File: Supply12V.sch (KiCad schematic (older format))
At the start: 31 parts, among them Q3 BSS138, Q5 CSD18504Q5A, Q6 CSD18504Q5A, U6 LM25116MHX

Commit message: Reannotated parts
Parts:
- renumbered C25 to C13, C19 to C14, C23 to C15, C13 to C16, C3 to C17, C20 to C18, C28 to C19, C11 to C20, C14 to C21, C21 to C22, D1 to D3, L1 to L2, Q5 to Q7, Q3 to Q8, Q6 to Q9, R33 to R59, R34 to R60, R16 to R61, R19 to R62, R23 to R63, R29 to R64, R17 to R65, R83 to R66, R36 to R67, R30 to R68, R24 to R69, R27 to R70, U6 to U1, W2 to W1, W1 to W2

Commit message: Silkscreen and 3D touchups
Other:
- moved on the sheet: C13, C14, C15, C16, C17, C18, C19, C20, C21, C22, D3, JP1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

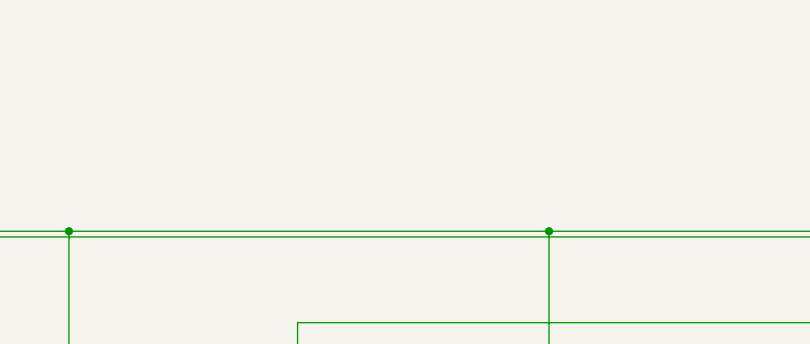
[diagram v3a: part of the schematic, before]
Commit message: Researched alternative DC-DC controllers
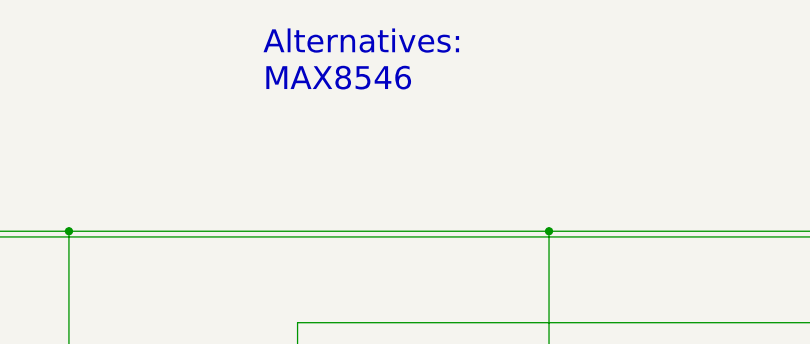
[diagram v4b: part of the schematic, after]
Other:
- note added: "Alternatives:\nMAX8546"
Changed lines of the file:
@@
 Wire Wire Line
 	1025 1425 1000 1400
+Text Notes 3550 800  0    100  ~ 0
+Alternatives:\nMAX8546
 $EndSCHEMATC

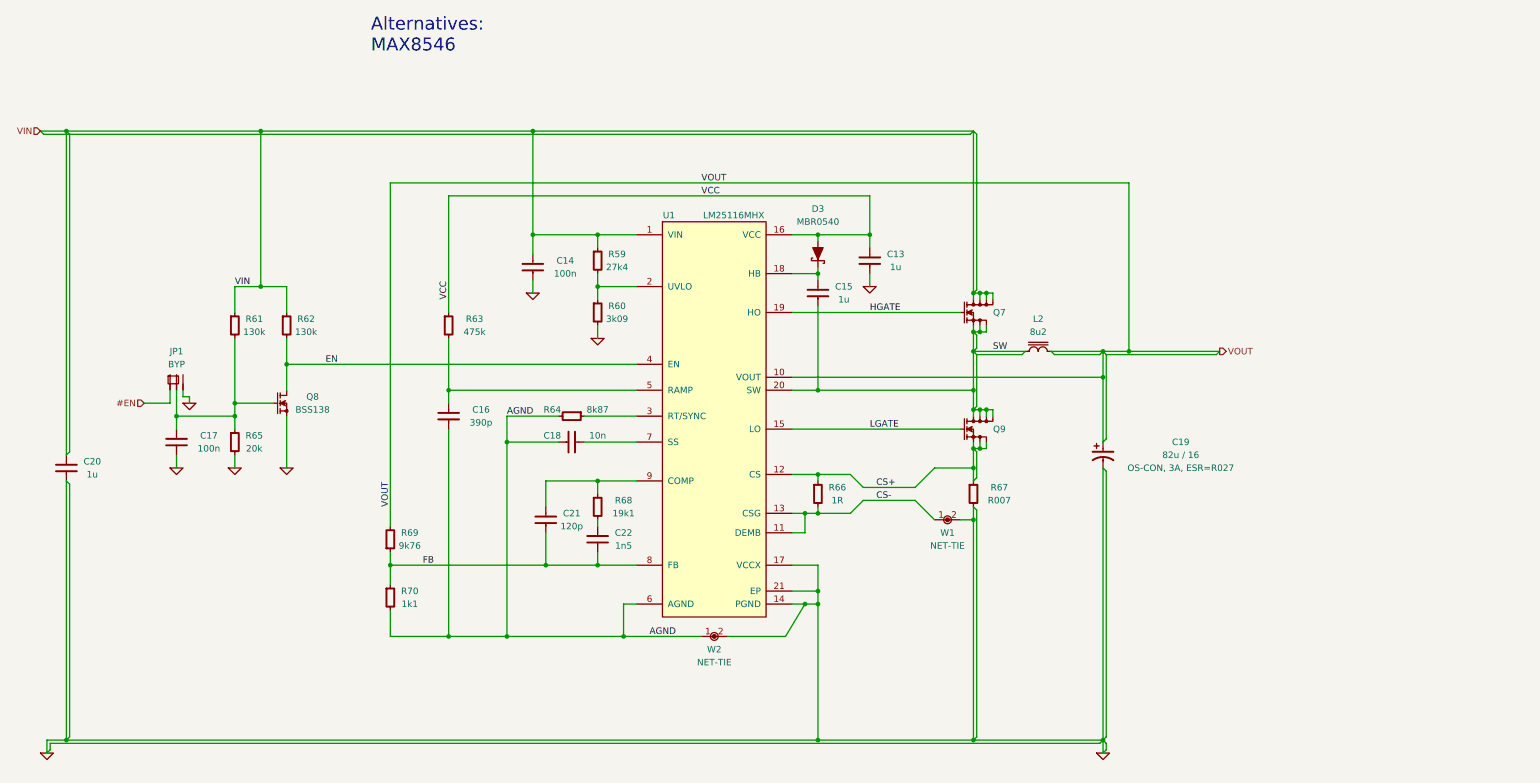
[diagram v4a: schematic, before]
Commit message: Changed BSS138 to MMUN221
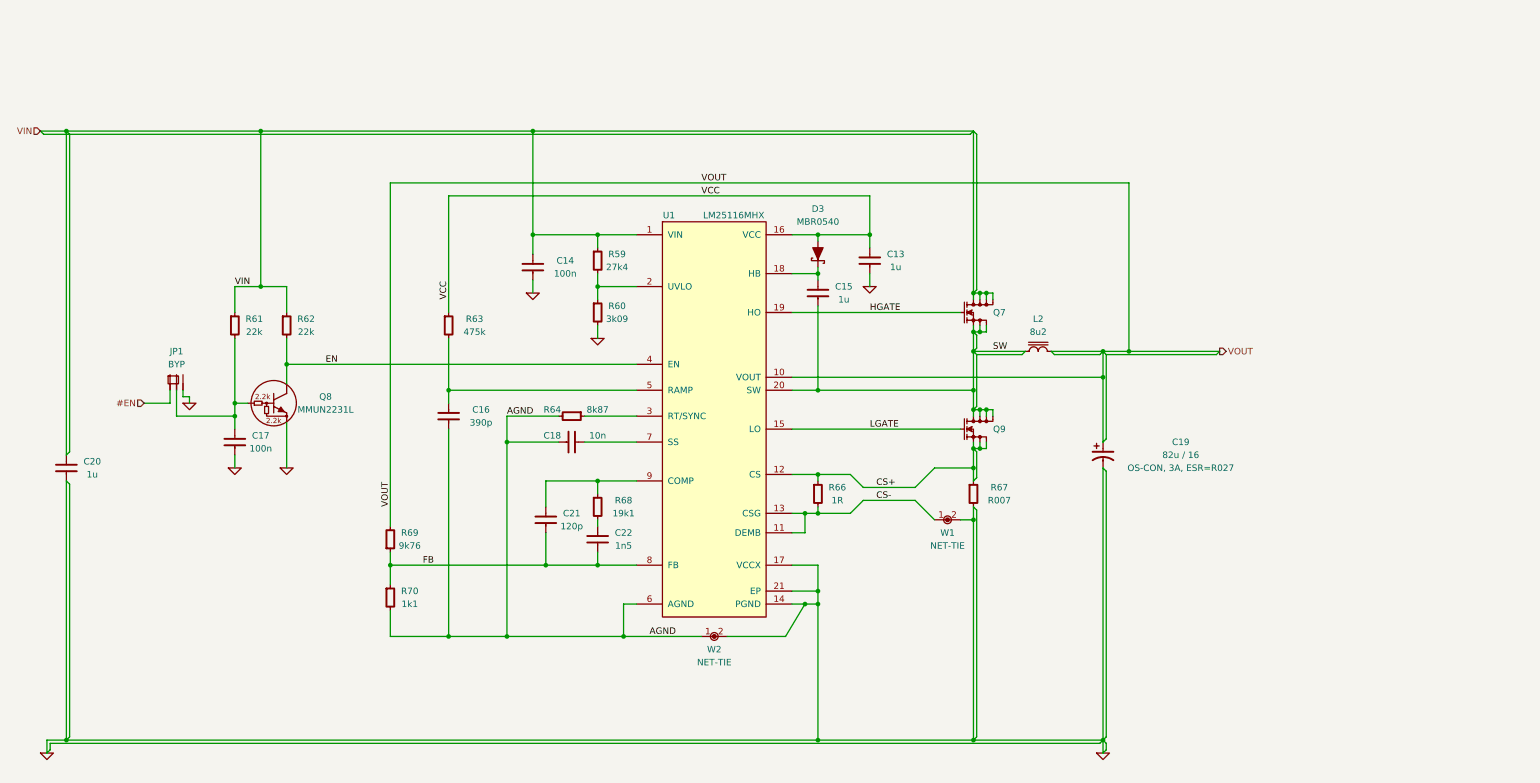
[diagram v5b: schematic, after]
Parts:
- removed Q8: BSS138, smd-semi:SOT-23, symbol BSS138
- removed R65: 20k, IPC7351-Nominal:RESC1005X40, symbol R-0402
- added Q8: MMUN2231L, smd-semi:SOT-23, symbol MMUN2231L
- R61, R62: value 130k -> 22k
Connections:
- net EN: now also Q8.3
- net GND: now also Q8.2
- net at C17.1, JP1.2, R61.2: now also Q8.1
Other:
- note removed: "Alternatives:\nMAX8546"
- moved on the sheet: C17
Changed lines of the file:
@@
-$EndComp
-$Comp
-L BSS138 Q8
-U 1 1 54D806F7
-P 2850 3500
-F 0 "Q8" H 3100 3550 50  0000 C CNN
-F 1 "BSS138" H 3100 3450 50  0000 C CNN
-F 2 "smd-semi:SOT-23" H 2850 3500 50  0001 C CNN
-F 3 "" H 2850 3500 60  0000 C CNN
-F 4 "Q3" H 2850 3500 50  0001 C CNN "OldReference"
-	1    2850 3500
-	1    0    0    -1
 $EndComp
 $Comp
@@
 P 2500 2900
 F 0 "R61" H 2650 2950 50  0000 C CNN
-F 1 "130k" H 2650 2850 50  0000 C CNN
+F 1 "22k" H 2650 2850 50  0000 C CNN
 F 2 "IPC7351-Nominal:RESC1005X40" H 2500 2900 50  0001 C CNN
 F 3 "" H 2500 2950 60  0000 C CNN
@@
 $EndComp
 $Comp
-L R-0402 R65
-U 1 1 54D80707
-P 2500 3800
-F 0 "R65" H 2650 3850 50  0000 C CNN
-F 1 "20k" H 2650 3750 50  0000 C CNN
-F 2 "IPC7351-Nominal:RESC1005X40" H 2500 3800 50  0001 C CNN
-F 3 "" H 2500 3850 60  0000 C CNN
-F 4 "R17" H 2500 3800 50  0001 C CNN "OldReference"
-	1    2500 3800
-	1    0    0    -1
-$EndComp
-$Comp
 L R-0402 R62
 U 1 1 54D8071F
 P 2900 2900
 F 0 "R62" H 3050 2950 50  0000 C CNN
-F 1 "130k" H 3050 2850 50  0000 C CNN
+F 1 "22k" H 3050 2850 50  0000 C CNN
 F 2 "IPC7351-Nominal:RESC1005X40" H 2900 2900 50  0001 C CNN
 F 3 "" H 2900 2950 60  0000 C CNN
@@
 L C-0805 C17
 U 1 1 54D8072E
-P 2050 3800
-F 0 "C17" H 2300 3850 50  0000 C CNN
-F 1 "100n" H 2300 3750 50  0000 C CNN
-F 2 "IPC7351-Nominal:CAPC2012X70" H 2050 3800 50  0001 C CNN
-F 3 "" H 2040 3775 60  0000 C CNN
-F 4 "C3" H 2050 3800 50  0001 C CNN "OldReference"
-	1    2050 3800
+P 2500 3800
+F 0 "C17" H 2700 3850 50  0000 C CNN
+F 1 "100n" H 2700 3750 50  0000 C CNN
+F 2 "IPC7351-Nominal:CAPC2012X70" H 2500 3800 50  0001 C CNN
+F 3 "" H 2490 3775 60  0000 C CNN
+F 4 "C3" H 2500 3800 50  0001 C CNN "OldReference"
+	1    2500 3800
 	1    0    0    -1
 $EndComp
@@
 	1    0    0    -1
 $EndComp
-$Comp
-L GND #PWR0225
-U 1 1 54DA9586
-P 2050 4000
-F 0 "#PWR0225" H 2050 4000 30  0001 C CNN
-F 1 "GND" H 2050 3930 30  0001 C CNN
-F 2 "" H 2050 4000 60  0000 C CNN
-F 3 "" H 2050 4000 60  0000 C CNN
-F 4 "#PWR0223" H 2050 4000 50  0001 C CNN "OldReference"
-	1    2050 4000
-	1    0    0    -1
-$EndComp
 Text HLabel 1000 1400 0    50   Input ~ 0
 VIN
@@
 VCC
 $Comp
-L GND #PWR0226
+L GND #PWR0225
 U 1 1 54DAF58D
 P 1050 6200
-F 0 "#PWR0226" H 1050 6200 30  0001 C CNN
+F 0 "#PWR0225" H 1050 6200 30  0001 C CNN
 F 1 "GND" H 1050 6130 30  0001 C CNN
 F 2 "" H 1050 6200 60  0000 C CNN
@@
 $EndComp
 Wire Wire Line
-	8200 2900 8200 2950
-Wire Wire Line
-	8200 2950 8200 3100
-Wire Wire Line
-	8200 3100 8200 3400
-Wire Wire Line
-	8200 3400 8200 3550
-Wire Wire Line
-	8200 3550 8200 3600
-Wire Wire Line
-	8200 3800 8200 3850
-Wire Wire Line
-	8200 3850 8200 4000
-Wire Wire Line
-	8200 4000 8200 4100
+	8200 2900 8200 3600
+Wire Wire Line
+	8200 3800 8200 4100
 Wire Wire Line
 	5300 4400 5300 4450
 Wire Wire Line
-	9200 4000 9200 6100
-Wire Wire Line
-	9200 6100 9200 6200
-Wire Wire Line
-	8200 1400 8200 2650
-Wire Wire Line
-	8200 2650 8200 2700
-Wire Wire Line
-	8200 2650 8250 2650
-Wire Wire Line
-	8250 2650 8300 2650
-Wire Wire Line
-	8300 2650 8350 2650
+	9200 4000 9200 6200
+Wire Wire Line
+	8200 1400 8200 2700
+Wire Wire Line
+	8200 2650 8350 2650
 Wire Wire Line
 	8250 2650 8250 2700
@@
 	8250 2900 8250 2950
 Wire Wire Line
-	8200 2950 8250 2950
-Wire Wire Line
-	8250 2950 8300 2950
+	8200 2950 8300 2950
 Connection ~ 8200 2950
 Wire Wire Line
@@
 Connection ~ 8250 2950
 Wire Wire Line
-	8200 3550 8250 3550
-Wire Wire Line
-	8250 3550 8300 3550
-Wire Wire Line
-	8300 3550 8350 3550
+	8200 3550 8350 3550
 Wire Wire Line
 	8250 3550 8250 3600
@@
 	8250 3800 8250 3850
 Wire Wire Line
-	8200 3850 8250 3850
-Wire Wire Line
-	8250 3850 8300 3850
+	8200 3850 8300 3850
 Connection ~ 8200 3850
 Wire Wire Line
@@
 Connection ~ 8250 3850
 Wire Wire Line
-	8800 3100 9200 3100
-Wire Wire Line
-	9200 3100 9400 3100
-Wire Wire Line
-	9400 3100 10100 3100
-Wire Wire Line
-	9200 3100 9200 3300
-Wire Wire Line
-	9200 3300 9200 3800
+	8800 3100 10100 3100
+Wire Wire Line
+	9200 3100 9200 3800
 Wire Wire Line
 	8600 3100 8200 3100
 Wire Wire Line
-	1050 6100 1200 6100
-Wire Wire Line
-	1200 6100 7000 6100
-Wire Wire Line
-	7000 6100 8200 6100
-Wire Wire Line
-	8200 6100 9200 6100
-Wire Wire Line
-	8200 4300 8200 4400
-Wire Wire Line
-	8200 4400 8200 6100
+	1050 6100 9200 6100
+Wire Wire Line
+	8200 4300 8200 6100
 Connection ~ 9200 6100
 Connection ~ 8200 3100
@@
 	1200 1400 1200 3900
 Wire Wire Line
-	1000 1400 1200 1400
-Wire Wire Line
-	1200 1400 2700 1400
-Wire Wire Line
-	2700 1400 4800 1400
-Wire Wire Line
-	4800 1400 8200 1400
+	1000 1400 8200 1400
 Connection ~ 1200 1400
 Connection ~ 1200 6100
@@
 	8100 4400 8200 4400
 Wire Wire Line
-	6800 3400 7000 3400
-Wire Wire Line
-	7000 3400 8200 3400
+	6800 3400 8200 3400
 Wire Wire Line
 	6800 3700 8100 3700
@@
 Connection ~ 7000 4950
 Wire Wire Line
-	7000 5050 6900 5050
-Wire Wire Line
-	6900 5050 6800 5050
+	7000 5050 6800 5050
 Connection ~ 7000 5050
 Wire Wire Line
@@
 	6800 2500 7000 2500
 Wire Wire Line
-	7000 2450 7000 2500
-Wire Wire Line
-	7000 2500 7000 2550
-Wire Wire Line
-	6800 2200 7000 2200
-Wire Wire Line
-	7000 2200 7400 2200
+	7000 2450 7000 2550
+Wire Wire Line
+	6800 2200 7400 2200
 Wire Wire Line
 	7000 2200 7000 2250
@@
 	7400 2600 7400 2500
 Wire Wire Line
-	7400 1900 7400 2200
-Wire Wire Line
-	7400 2200 7400 2300
+	7400 1900 7400 2300
 Connection ~ 7000 2200
 Wire Wire Line
-	5300 2500 5300 2600
-Wire Wire Line
-	5300 2600 5300 2700
+	5300 2500 5300 2700
 Wire Wire Line
 	5300 2600 5600 2600
@@
 	7350 4150 7250 4050
 Wire Wire Line
-	7250 4050 7000 4050
-Wire Wire Line
-	7000 4050 6800 4050
+	7250 4050 6800 4050
 Wire Wire Line
 	7000 4100 7000 4050
@@
 	7350 4250 7250 4350
 Wire Wire Line
-	7250 4350 7000 4350
-Wire Wire Line
-	7000 4350 6900 4350
-Wire Wire Line
-	6900 4350 6800 4350
+	7250 4350 6800 4350
 Wire Wire Line
 	7000 4300 7000 4350
@@
 Connection ~ 6900 5050
 Wire Wire Line
-	3700 5300 4150 5300
-Wire Wire Line
-	4150 5300 4600 5300
-Wire Wire Line
-	4600 5300 5500 5300
-Wire Wire Line
-	5500 5300 6100 5300
+	3700 5300 6100 5300
 Wire Wire Line
 	5500 5300 5500 5050
@@
 	5500 5050 5600 5050
 Wire Wire Line
-	4900 4100 5300 4100
-Wire Wire Line
-	5300 4100 5600 4100
+	4900 4100 5600 4100
 Wire Wire Line
 	4900 4100 4900 4300
@@
 	5300 4750 5300 4650
 Wire Wire Line
-	3700 4750 4900 4750
-Wire Wire Line
-	4900 4750 5300 4750
-Wire Wire Line
-	5300 4750 5600 4750
+	3700 4750 5600 4750
 Wire Wire Line
 	4900 4750 4900 4500
@@
 Connection ~ 5500 5300
 Wire Wire Line
-	3700 4650 3700 4750
-Wire Wire Line
-	3700 4750 3700 4900
+	3700 4650 3700 4900
 Connection ~ 4900 4750
 Connection ~ 3700 4750
@@
 	5000 3600 4600 3600
 Wire Wire Line
-	4600 3600 4600 3800
-Wire Wire Line
-	4600 3800 4600 5300
+	4600 3600 4600 5300
 Connection ~ 4600 5300
 Wire Wire Line
@@
 Connection ~ 4150 5300
 Wire Wire Line
-	4150 3000 4150 3400
-Wire Wire Line
-	4150 3400 4150 3500
+	4150 3000 4150 3500
 Wire Wire Line
 	4150 3400 5600 3400
@@
 	5600 3200 2900 3200
 Wire Wire Line
-	2900 3000 2900 3200
-Wire Wire Line
-	2900 3200 2900 3400
+	2900 3000 2900 3350
 Connection ~ 2900 3200
 Wire Wire Line
-	2500 3000 2500 3500
-Wire Wire Line
-	2500 3500 2500 3600
-Wire Wire Line
-	2500 3600 2500 3700
-Wire Wire Line
-	2500 3500 2800 3500
+	2500 3500 2600 3500
 Connection ~ 2500 3500
 Wire Wire Line
 	2500 3600 2050 3600
-Wire Wire Line
-	2050 3400 2050 3600
-Wire Wire Line
-	2050 3600 2050 3700
 Connection ~ 2500 3600
-Connection ~ 2050 3600
 Wire Wire Line
 	2100 3400 2100 3450
@@
 	2000 3500 2000 3400
 Wire Wire Line
-	2900 3600 2900 4000
-Wire Wire Line
-	2500 4000 2500 3900
-Wire Wire Line
-	2050 4000 2050 3900
+	2900 3650 2900 4000
 Wire Wire Line
 	2500 2800 2500 2600
 Wire Wire Line
-	2500 2600 2700 2600
-Wire Wire Line
-	2700 2600 2900 2600
+	2500 2600 2900 2600
 Wire Wire Line
 	2900 2600 2900 2800
@@
 Connection ~ 2700 2600
 Wire Wire Line
-	4800 1400 4800 2200
-Wire Wire Line
-	4800 2200 4800 2350
+	4800 1400 4800 2350
 Connection ~ 4800 2200
 Connection ~ 4800 1400
 Wire Wire Line
-	4800 2200 5300 2200
-Wire Wire Line
-	5300 2200 5600 2200
+	4800 2200 5600 2200
 Connection ~ 2700 1400
 Wire Wire Line
@@
 Connection ~ 6900 4350
 Wire Wire Line
-	7000 4750 7000 4950
-Wire Wire Line
-	7000 4950 7000 5050
-Wire Wire Line
-	7000 5050 7000 6100
+	7000 4750 7000 6100
 Wire Wire Line
 	1025 1425 1000 1400
-Text Notes 3550 800  0    100  ~ 0
-Alternatives:\nMAX8546
+$Comp
+L MMUN2231L Q8
+U 1 1 54D950A4
+P 2850 3500
+F 0 "Q8" H 3200 3550 50  0000 C CNN
+F 1 "MMUN2231L" H 3200 3450 50  0000 C CNN
+F 2 "smd-semi:SOT-23" H 2850 3500 50  0001 C CNN
+F 3 "" H 2850 3500 60  0000 C CNN
+	1    2850 3500
+	1    0    0    -1
+$EndComp
+Wire Wire Line
+	2500 4000 2500 3900
+Wire Wire Line
+	2500 3000 2500 3700
+Wire Wire Line
+	2050 3600 2050 3400
 $EndSCHEMATC
